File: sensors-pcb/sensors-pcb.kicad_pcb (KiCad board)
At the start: 2 copper layers, 75 x 55 mm, 41 parts, among them J1 Network Connector, J2 STDC14, SW1 SW_Push, U1 LD39050PU33R, U2 STM32G474RBT6, U3 SN65HVD230, Y1 8MHz

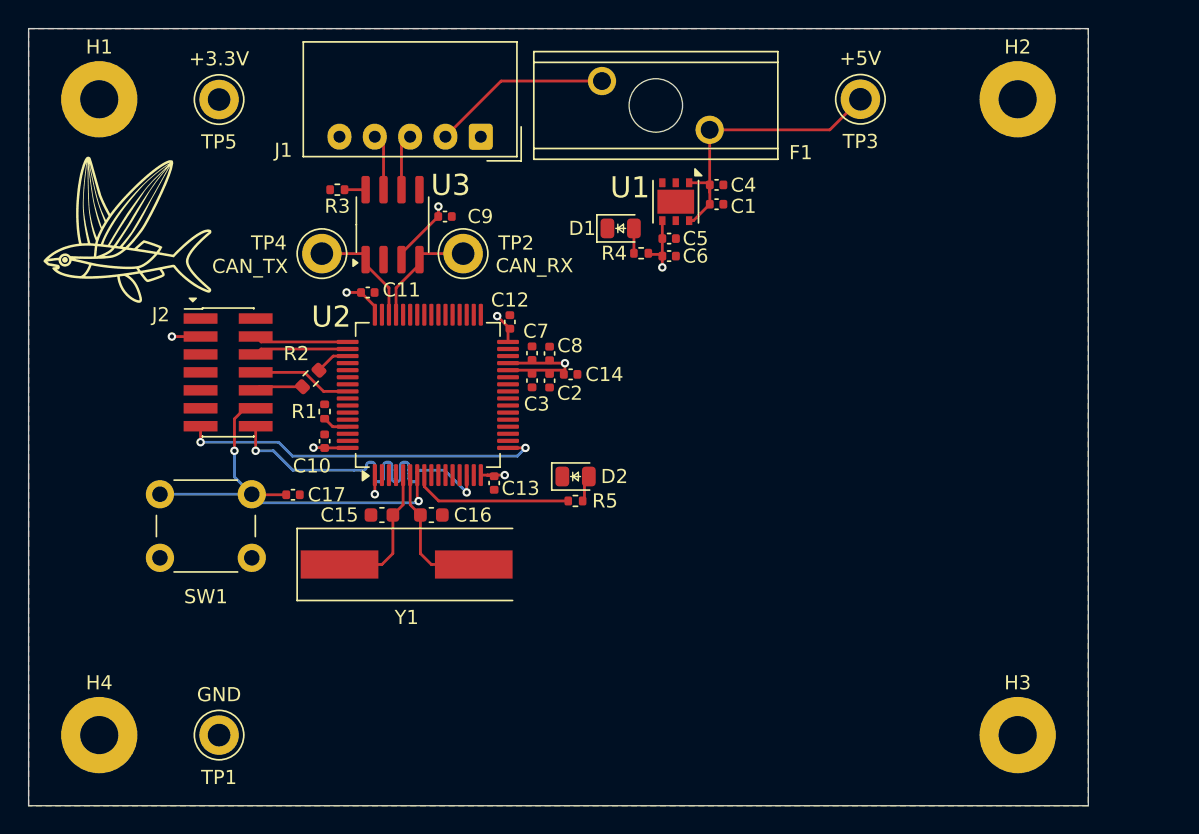
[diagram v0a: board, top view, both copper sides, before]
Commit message: sensors-pcb: add footprints
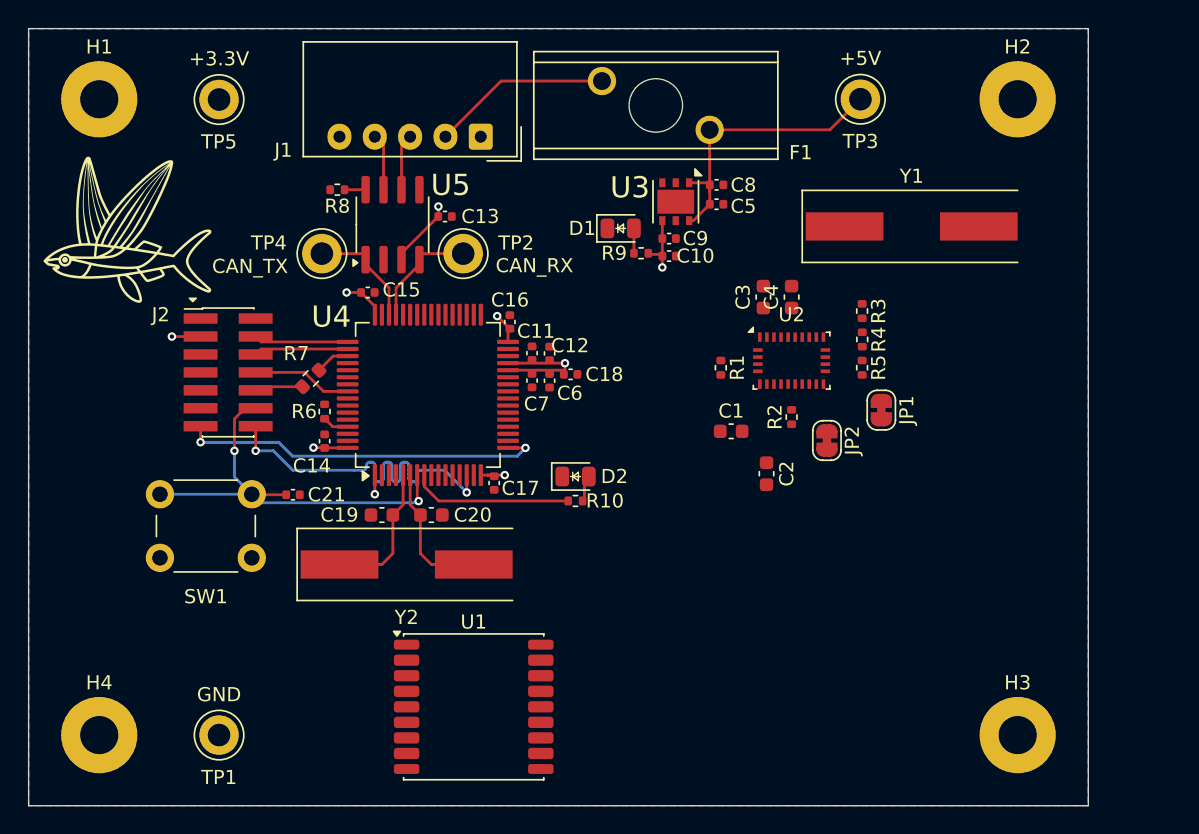
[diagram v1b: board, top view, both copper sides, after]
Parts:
- added C1: 100n, Capacitor_SMD:C_0603_1608Metric, F.Cu at (239.7, 50.0)
- added C2: 100n, Capacitor_SMD:C_0603_1608Metric, F.Cu at (242.2, 53.0)
- added C3: 22p, Capacitor_SMD:C_0603_1608Metric, F.Cu at (242.0, 40.5)
- added C4: 22p, Capacitor_SMD:C_0603_1608Metric, F.Cu at (244.0, 40.5)
- added JP1: SolderJumper_2_Open, Jumper:SolderJumper-2_P1.3mm_Bridged_RoundedPad1.0x1.5mm, F.Cu at (250.3, 48.5)
- added JP2: SolderJumper_2_Open, Jumper:SolderJumper-2_P1.3mm_Bridged_RoundedPad1.0x1.5mm, F.Cu at (246.5, 50.6)
- added R1: 10k, Resistor_SMD:R_0402_1005Metric, F.Cu at (239.0, 45.5)
- added R2: 10k, Resistor_SMD:R_0402_1005Metric, F.Cu at (244.0, 49.0)
- added R3: 10k, Resistor_SMD:R_0402_1005Metric, F.Cu at (249.0, 41.5)
- added R4: 10k, Resistor_SMD:R_0402_1005Metric, F.Cu at (249.0, 43.5)
- added R5: 40k, Resistor_SMD:R_0402_1005Metric, F.Cu at (249.0, 45.5)
- added U1: MAX-M8Q, RF_GPS:ublox_MAX, F.Cu at (221.5, 69.5)
- added U2: BNO055, Package_LGA:LGA-28_5.2x3.8mm_P0.5mm, F.Cu at (244.0, 45.0)
- added Y1: 32kHz, Exocet:Crystal_SMD_HC49-SD, F.Cu at (252.5, 35.5)
- renumbered C6 to C10, C7 to C11, C8 to C12, C9 to C13, C10 to C14, C11 to C15, C12 to C16, C13 to C17, C14 to C18, C15 to C19, C16 to C20, C17 to C21, C1 to C5, C2 to C6, C3 to C7, C4 to C8, C5 to C9, R5 to R10, R1 to R6, R2 to R7, R3 to R8, R4 to R9, U1 to U3, U2 to U4, U3 to U5, Y1 to Y2
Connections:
- U4 pad 22: unconnected-(U2-PC4-Pad22) -> /SCL_IMU
- U4 pad 40: unconnected-(U2-PC8-Pad40) -> /STM32 Base Layout/I2C3_SCL
- U4 pad 41: unconnected-(U2-PC9-Pad41) -> /STM32 Base Layout/I2C3_SDA
- U4 pad 42: unconnected-(U2-PA8-Pad42) -> /SDA_IMU

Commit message: sensors-pcb: route IMU
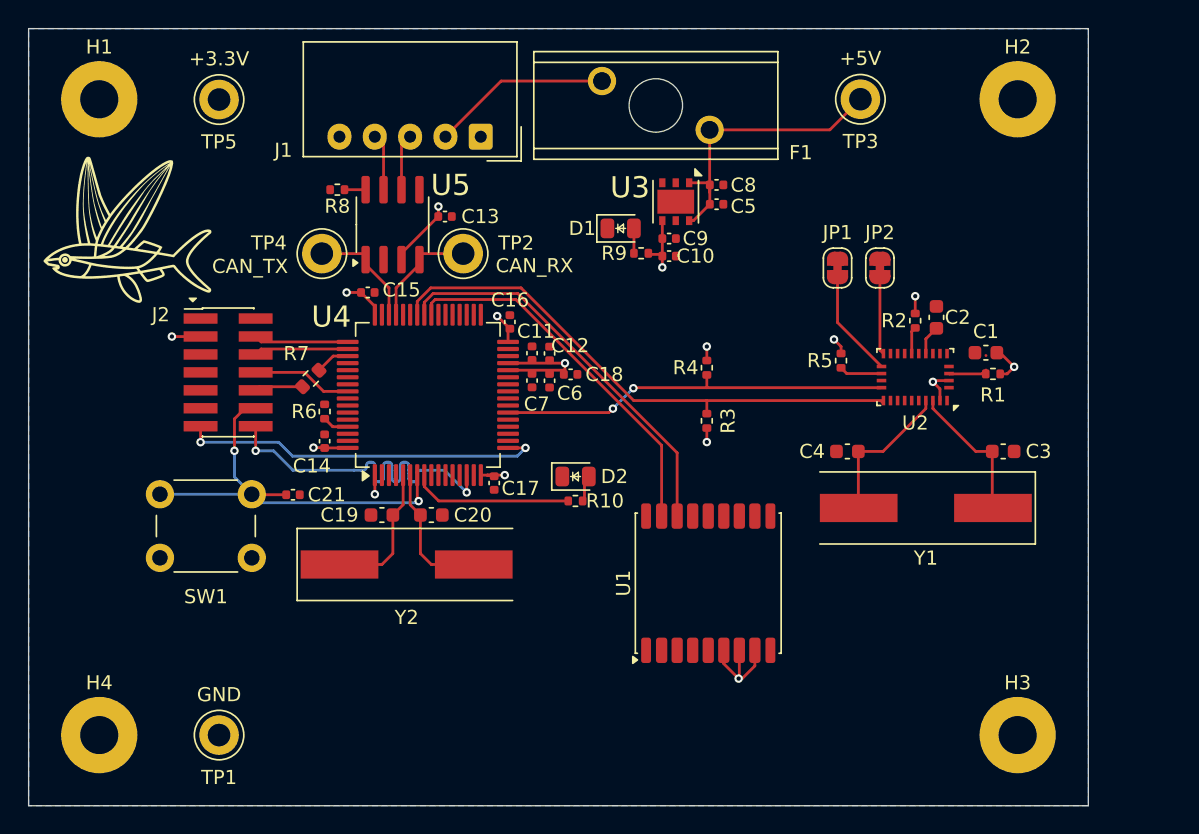
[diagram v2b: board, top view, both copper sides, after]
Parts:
- moved C3 20.2 mm to (259.0, 51.4), turned to 0 degrees
- moved Y1 20.0 mm to (253.5, 55.4), turned to 180 degrees
- moved R1 19.3 mm to (258.2, 45.9), turned to 0 degrees
- moved C1 18.9 mm to (257.8, 44.4), turned to 180 degrees
- moved U1 18.8 mm to (238.1, 60.8), turned to 90 degrees
- moved C2 16.3 mm to (254.2, 41.9), turned to 90 degrees
- moved R3 13.5 mm to (238.0, 49.3)
- moved JP2 12.8 mm to (250.2, 38.4), turned to 90 degrees
- moved C4 11.6 mm to (247.9, 51.4), turned to 180 degrees
- moved R4 11.2 mm to (238.0, 45.5), turned to 90 degrees
- moved R2 11.1 mm to (252.8, 42.2), turned to -90 degrees
- moved JP1 10.5 mm to (247.2, 38.4), turned to 90 degrees
- moved U2 8.83 mm to (252.8, 46.2), turned to 180 degrees
- moved R5 1.57 mm to (247.5, 45.0), turned to 90 degrees
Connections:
- U4 pad 40: /STM32 Base Layout/I2C3_SCL -> /SCL_GPS
- U4 pad 41: /STM32 Base Layout/I2C3_SDA -> /SDA_GPS
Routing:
- net /SDA_IMU: track 0.00 -> 38.7 mm
- net /SDA_GPS: track 0.00 -> 28.2 mm
- net /SCL_IMU: track 0.00 -> 28.1 mm, vias 0 -> 2
- net /SCL_GPS: track 0.00 -> 26.5 mm
- net +3.3V: track 30.4 -> 47.4 mm, vias 9 -> 16
- net /OSC_OUT: track 0.00 -> 10.6 mm
- net /OSC_IN: track 0.00 -> 10.1 mm
- net Net-(JP1-A): track 0.00 -> 7.61 mm
- net Net-(JP2-A): track 0.00 -> 5.52 mm
- net Net-(U2-COM3): track 0.00 -> 3.03 mm
- net Net-(U2-nBOOT_LOAD_PIN): track 0.00 -> 2.97 mm
- net Net-(U2-CAP): track 0.00 -> 2.10 mm
- net Net-(U2-~{nReset}): track 0.00 -> 1.92 mm
- removed copper zone on F.Cu, net GND

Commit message: sensors-pcb: readded ground plane
oups :P
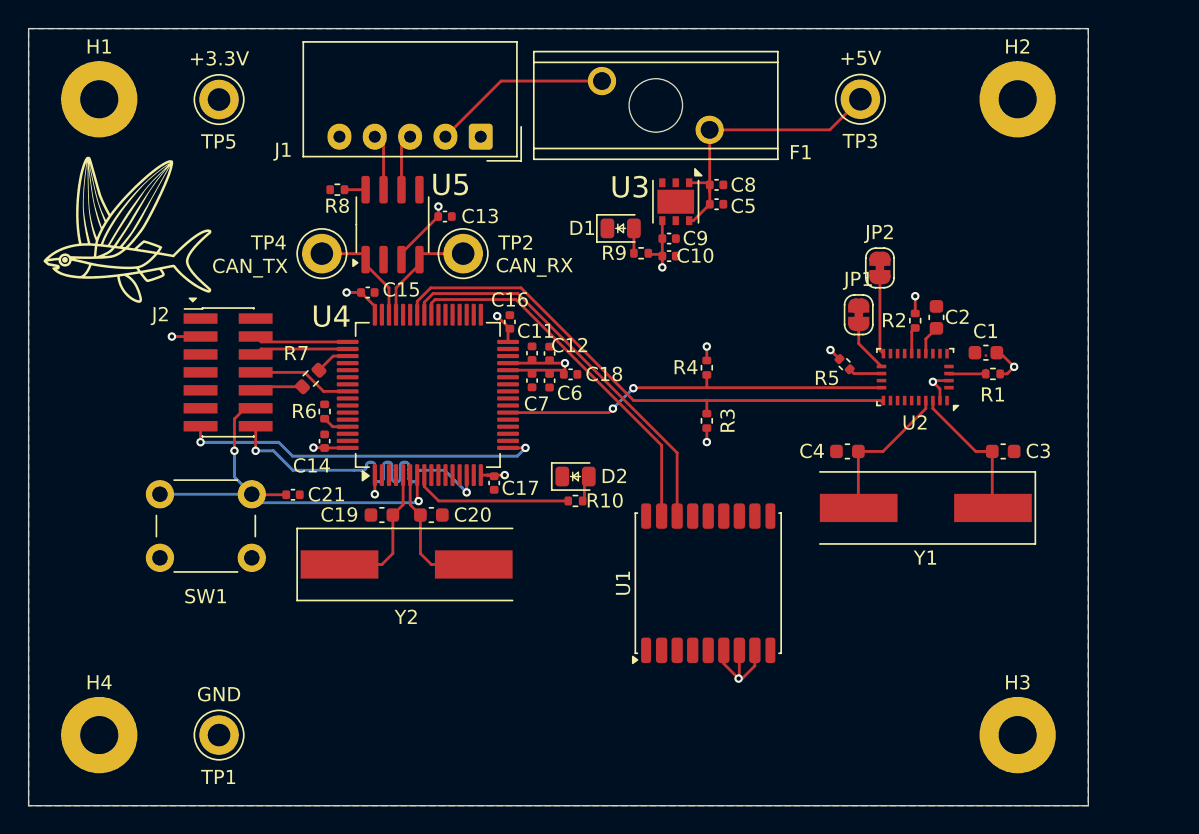
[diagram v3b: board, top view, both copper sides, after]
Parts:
- moved JP1 3.64 mm to (248.8, 41.8)
- moved R5 0.35 mm to (247.8, 45.2), turned to 135 degrees
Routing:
- net Net-(JP1-A): track 7.61 -> 3.68 mm
- net Net-(U2-COM3): track 3.03 -> 2.38 mm
- added copper zone on F.Cu, net GND
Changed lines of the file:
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@@
 	(footprint "Jumper:SolderJumper-2_P1.3mm_Bridged_RoundedPad1.0x1.5mm"
 		(layer "F.Cu")
-		(at 247.25 38.4375 90)
+		(at 248.75 41.75 90)
 		(descr "SMD Solder Jumper, 1x1.5mm, rounded Pads, 0.3mm gap, bridged with 1 copper strip")
 		(tags "net tie solder jumper bridged")
@@
 	(footprint "Resistor_SMD:R_0402_1005Metric"
 		(layer "F.Cu")
-		(at 247.5 45 90)
+		(at 247.75 45.25 135)
 		(descr "Resistor SMD 0402 (1005 Metric), square (rectangular) end terminal, IPC-7351 nominal, (Body size source: IPC-SM-782 page 72, https://www.pcb-3d.com/wordpress/wp-content/uploads/ipc-sm-782a_amendment_1_and_2.pdf), generated with kicad-footprint-generator")
 		(tags "resistor")
 		(property "Reference" "R5"
-			(at 0 -1.5 180)
+			(at 0.176777 -1.59099 0)
 			(layer "F.SilkS")
 			(effects
@@
 		)
 		(property "Value" "40k"
-			(at 0 0 90)
+			(at 0 0 135)
 			(layer "F.Fab")
 			(effects
@@
 		)
 		(property "Datasheet" "~"
-			(at 0 0 90)
+			(at 0 0 135)
 			(layer "F.Fab")
 			(hide yes)
@@
 		)
 		(property "Description" "Resistor"
-			(at 0 0 90)
+			(at 0 0 135)
 			(layer "F.Fab")
 			(hide yes)
@@
 		)
 		(fp_line
-			(start -0.93 -0.47)
-			(end 0.93 -0.47)
+			(start 0.93 0.47)
+			(end -0.93 0.47)
 			(stroke
 				(width 0.05)
@@
 		)
 		(fp_line
-			(start 0.93 0.47)
-			(end -0.93 0.47)
+			(start -0.93 -0.47)
+			(end 0.93 -0.47)
 			(stroke
 				(width 0.05)
@@
 		)
 		(fp_line
-			(start -0.525 -0.27)
-			(end 0.525 -0.27)
+			(start 0.525 0.27)
+			(end -0.525 0.27)
 			(stroke
 				(width 0.1)
@@
 		)
 		(fp_line
-			(start 0.525 0.27)
-			(end -0.525 0.27)
+			(start -0.525 -0.27)
+			(end 0.525 -0.27)
 			(stroke
 				(width 0.1)
@@
 		)
 		(pad "1" smd roundrect
-			(at -0.51 0 90)
+			(at -0.509999 0 135)
 			(size 0.54 0.64)
 			(layers "F.Cu" "F.Mask" "F.Paste")
@@
 		)
 		(pad "2" smd roundrect
-			(at 0.51 0 90)
+			(at 0.509999 0 135)
 			(size 0.54 0.64)
 			(layers "F.Cu" "F.Mask" "F.Paste")
@@
 	)
 	(segment
-		(start 247.5 44)
-		(end 247 43.5)
-		(width 0.2)
-		(layer "F.Cu")
-		(net 3)
-	)
-	(segment
 		(start 239.2 65.5)
 		(end 239.2 66.45)
@@
 	)
 	(segment
-		(start 247.5 44.49)
-		(end 247.5 44)
-		(width 0.2)
-		(layer "F.Cu")
-		(net 3)
-	)
-	(segment
 		(start 259.25 45.9375)
 		(end 259.75 45.4375)
@@
 	)
 	(segment
+		(start 246.75 44.25)
+		(end 247.389376 44.889376)
+		(width 0.2)
+		(layer "F.Cu")
+		(net 3)
+	)
+	(segment
 		(start 234.85 35.09)
 		(end 234.85 38.4)
@@
 	)
 	(via
-		(at 247 43.5)
+		(at 246.75 44.25)
 		(size 0.6)
 		(drill 0.3)
@@
 	)
 	(segment
-		(start 247.25 39.0875)
-		(end 247.25 42.3)
+		(start 248.75 43.8)
+		(end 250.3625 45.4125)
 		(width 0.2)
 		(layer "F.Cu")
@@
 	)
 	(segment
-		(start 247.25 42.3)
-		(end 250.3625 45.4125)
+		(start 248.75 42.4)
+		(end 248.75 43.8)
 		(width 0.2)
 		(layer "F.Cu")
@@
 	)
 	(segment
-		(start 247.9025 45.9125)
-		(end 250.3625 45.9125)
+		(start 248.110624 45.610624)
+		(end 248.4125 45.9125)
 		(width 0.2)
 		(layer "F.Cu")
@@
 	)
 	(segment
-		(start 247.5 45.51)
-		(end 247.9025 45.9125)
+		(start 248.4125 45.9125)
+		(end 250.3625 45.9125)
 		(width 0.2)
 		(layer "F.Cu")
@@
 	)
 	(zone
+		(net 1)
+		(net_name "GND")
+		(layer "F.Cu")
+		(hatch edge 0.5)
+		(connect_pads
+			(clearance 0.2)
+		)
+		(min_thickness 0.25)
+		(filled_areas_thickness no)
+		(fill yes
+			(thermal_gap 0.5)
+			(thermal_bridge_width 0.5)
+		)
+		(polygon
+			(pts
+				(xy 265 21.5) (xy 265 76.5) (xy 190 76.5) (xy 190 21.5)
+			)
+		)
+	)
+	(zone

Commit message: sensors-pcb: add coax connector, link JLCPCB numbers
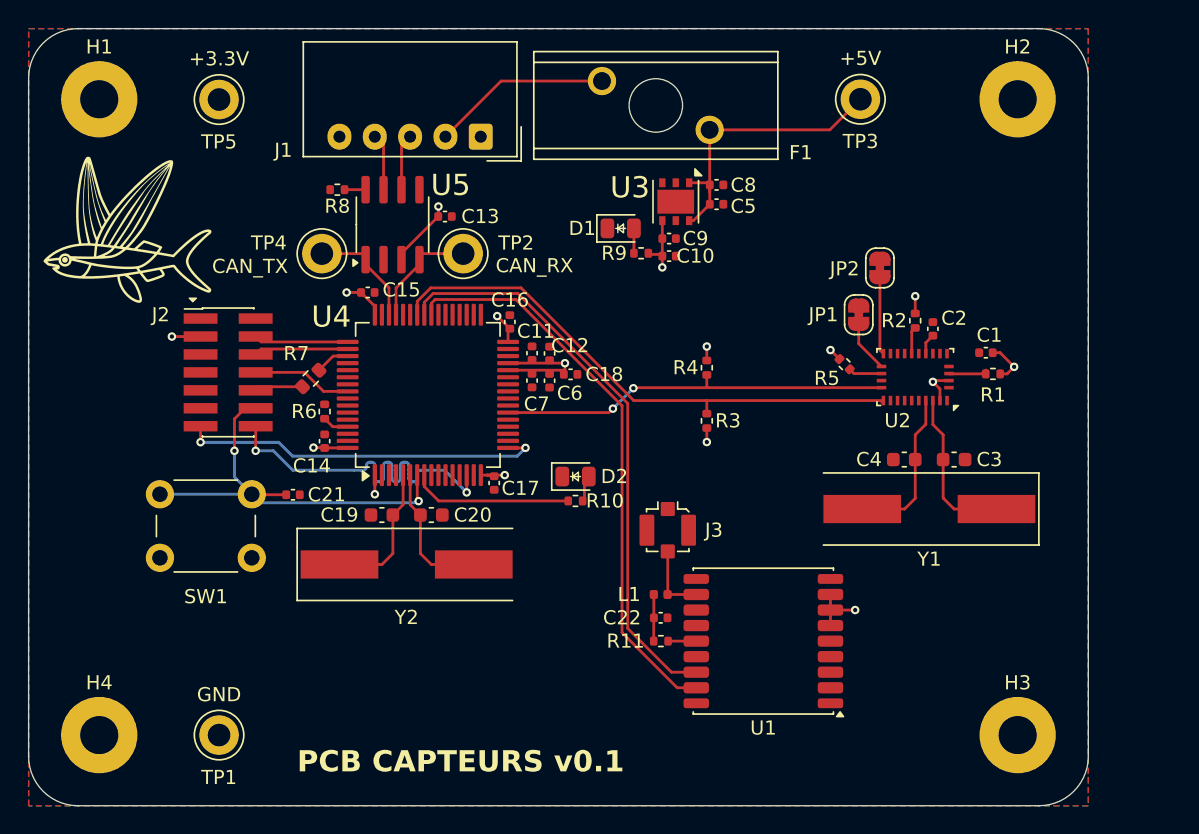
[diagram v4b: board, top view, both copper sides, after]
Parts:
- added C22: 10n, Capacitor_SMD:C_0402_1005Metric, F.Cu at (234.7, 63.2)
- added J3: Conn_Coaxial, Connector_Coaxial:U.FL_Molex_MCRF_73412-0110_Vertical, F.Cu at (235.2, 57.0)
- added L1: 27n, Inductor_SMD:L_0402_1005Metric, F.Cu at (234.7, 61.5)
- added R11: 10, Resistor_SMD:R_0402_1005Metric, F.Cu at (234.8, 64.8)
- C1, C2: footprint Capacitor_SMD:C_0603_1608Metric -> Capacitor_SMD:C_0402_1005Metric
- moved U1 5.66 mm to (242.0, 64.8), turned to 180 degrees
- moved C4 4.07 mm to (252.0, 52.0)
- moved C3 3.52 mm to (255.5, 52.0)
- moved C2 0.85 mm to (254.0, 42.8)
- moved Y1 0.26 mm to (253.8, 55.5)
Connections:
- U1 pad 14: unconnected-(U1-VCC_RF-Pad14) -> Net-(U1-VCC_RF)
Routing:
- net /SCL_GPS: track 26.5 -> 40.5 mm
- net /SDA_GPS: track 28.2 -> 40.8 mm
- net Net-(J3-In): track 0.00 -> 5.09 mm
- net Net-(C22-Pad1): track 0.00 -> 3.31 mm
- net +3.3V: track 47.1 -> 44.3 mm
- net Net-(U1-VCC_RF): track 0.00 -> 1.99 mm
- net /OSC_IN: track 10.1 -> 11.6 mm
- net /OSC_OUT: track 10.6 -> 11.6 mm
- net Net-(U2-CAP): track 2.10 -> 1.48 mm
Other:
- outline, holes or cut-outs redrawn
- board text added: "PCB CAPTEURS v0.1"

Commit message: sensors-pcb: fix the stuff
Ajouté des test points
Ajusté la longueur de la trace SCL_IMU
Ajouté condensateur de découplage pour le GPS
Mis a jour la metadata
Changé les solder jumpers
Reglé problèmes DRC. Il en reste 3 mais c'est lié au template et je sais pas trop comment les regler
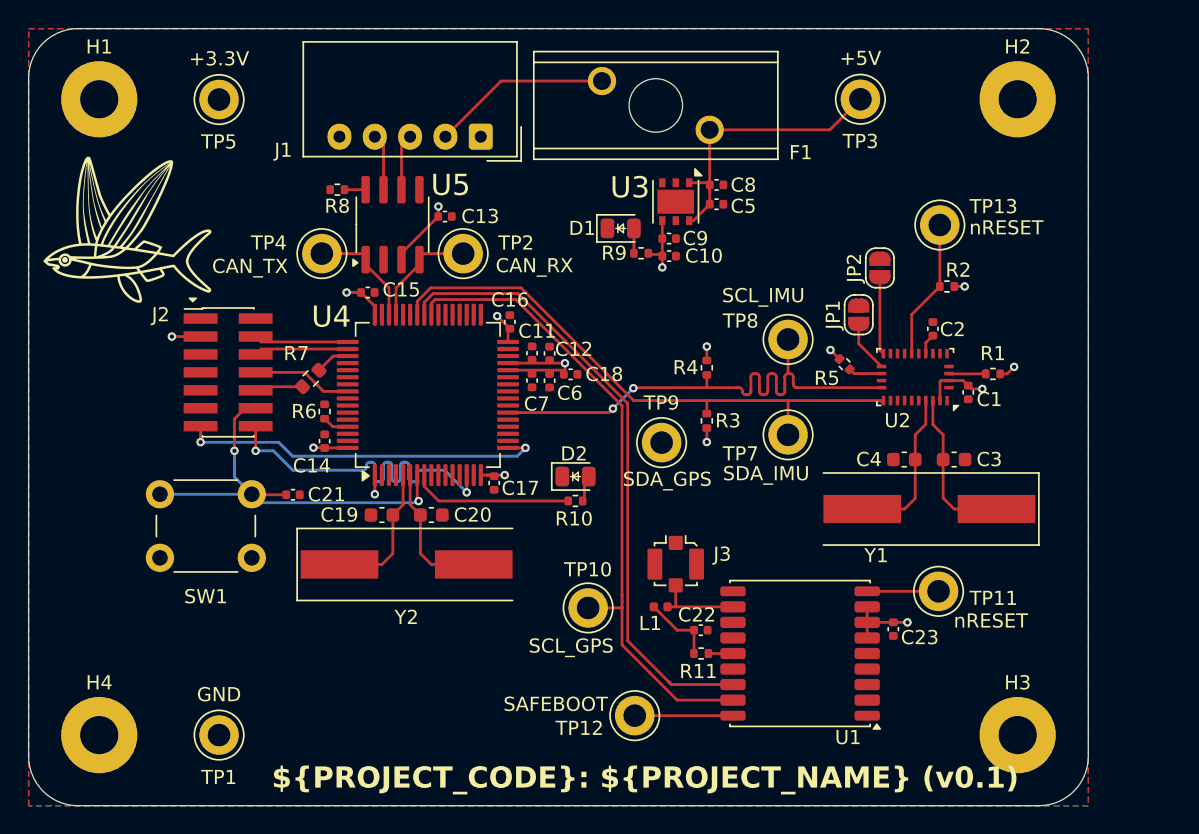
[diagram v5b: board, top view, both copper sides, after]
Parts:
- added C23: 100n, Capacitor_SMD:C_0402_1005Metric, F.Cu at (251.2, 64.0)
- added TP10: TestPoint, TestPoint:TestPoint_Keystone_5005-5009_Compact, F.Cu at (229.6, 62.5)
- added TP11: TestPoint, TestPoint:TestPoint_Keystone_5005-5009_Compact, F.Cu at (254.4, 61.3)
- added TP12: TestPoint, TestPoint:TestPoint_Keystone_5005-5009_Compact, F.Cu at (232.9, 70.1)
- added TP13: TestPoint, TestPoint:TestPoint_Keystone_5005-5009_Compact, F.Cu at (254.5, 35.4)
- added TP7: TestPoint, TestPoint:TestPoint_Keystone_5005-5009_Compact, F.Cu at (243.8, 50.2)
- added TP8: TestPoint, TestPoint:TestPoint_Keystone_5005-5009_Compact, F.Cu at (243.8, 43.5)
- added TP9: TestPoint, TestPoint:TestPoint_Keystone_5005-5009_Compact, F.Cu at (234.8, 50.8)
- JP1, JP2: footprint Jumper:SolderJumper-2_P1.3mm_Bridged_RoundedPad1.0x1.5mm -> Jumper:SolderJumper-2_P1.3mm_Open_RoundedPad1.0x1.5mm
- moved R2 3.31 mm to (255.0, 39.8), turned to 180 degrees
- moved C1 3.08 mm to (256.5, 47.2), turned to -90 degrees
- moved R11 2.98 mm to (237.6, 65.7)
- moved C22 2.97 mm to (237.6, 64.1)
- moved U1 2.74 mm to (244.6, 65.7)
- moved J3 2.47 mm to (235.8, 59.4)
- moved L1 0.88 mm to (234.7, 62.4)
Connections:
- U1 pad 18: unconnected-(U1-~{SAFEBOOT}-Pad18) -> Net-(U1-~{SAFEBOOT})
- U1 pad 9: unconnected-(U1-~{RESET}-Pad9) -> Net-(U1-~{RESET})
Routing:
- net /SCL_IMU: track 28.1 -> 37.9 mm
- net Net-(U2-~{nReset}): track 1.92 -> 9.92 mm
- net Net-(U1-~{SAFEBOOT}): track 0.00 -> 6.95 mm
- net /SCL_GPS: track 40.5 -> 46.3 mm
- net Net-(U1-~{RESET}): track 0.00 -> 5.05 mm
- net /SDA_GPS: track 40.8 -> 44.6 mm
- net /SDA_IMU: track 38.7 -> 41.1 mm
- net Net-(C22-Pad1): track 3.31 -> 5.18 mm
- net Net-(J3-In): track 5.09 -> 6.15 mm
- net +3.3V: track 44.3 -> 44.9 mm
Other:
- board text added: "${PROJECT_CODE}: ${PROJECT_NAME} (v0.1)"
- board text added: "${REFERENCE}"
- board text removed: "PCB CAPTEURS v0.1"

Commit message: sensors-pcb: update resistor
J'avais déjà associé la résistance 40k avec un code JLCPCB pour une 40.2k et elle semble être accessible donc voilà
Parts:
- R5: value 40k -> 40.2k
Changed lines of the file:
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@@
 			)
 		)
-		(property "Value" "40k"
+		(property "Value" "40.2k"
 			(at 0 0 135)
 			(layer "F.Fab")
